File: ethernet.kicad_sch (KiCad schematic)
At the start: 57 parts, among them J4 WE-RJ45_7499111121A, U9 KSZ9031RNXCA, Y1 ABM8G-25.000MHZ-18-D2Y-T

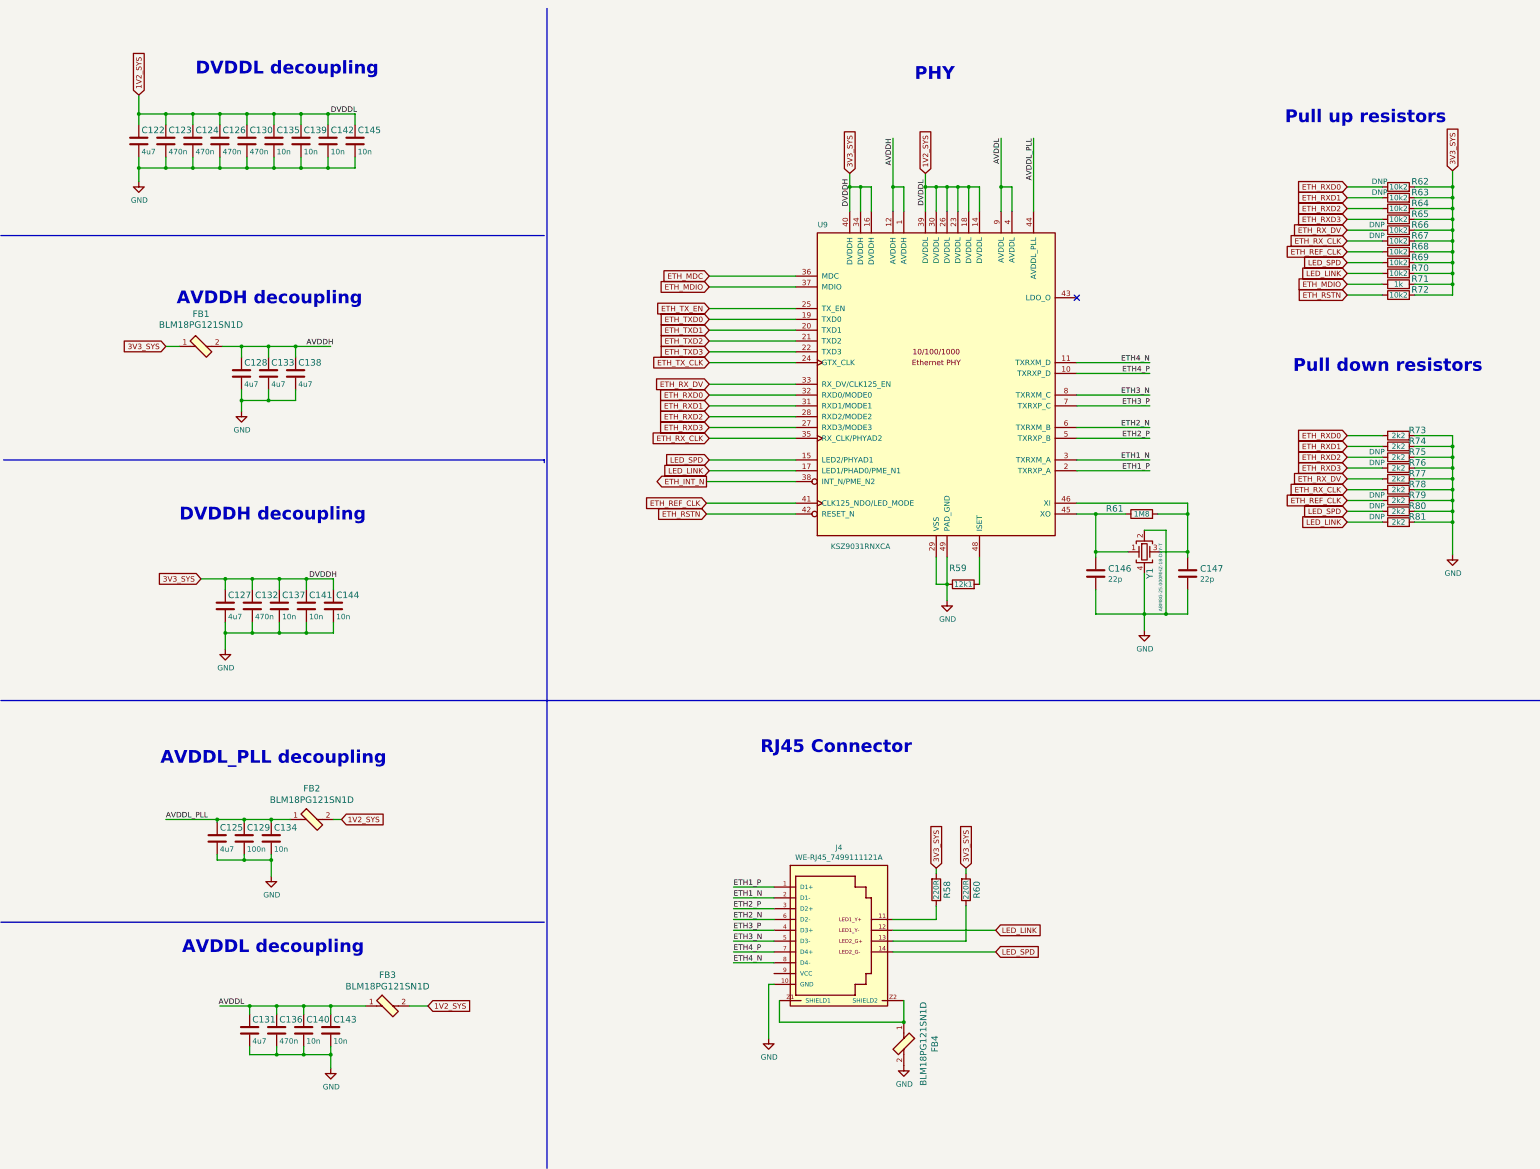
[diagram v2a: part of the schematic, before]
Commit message: Introduce component standarization
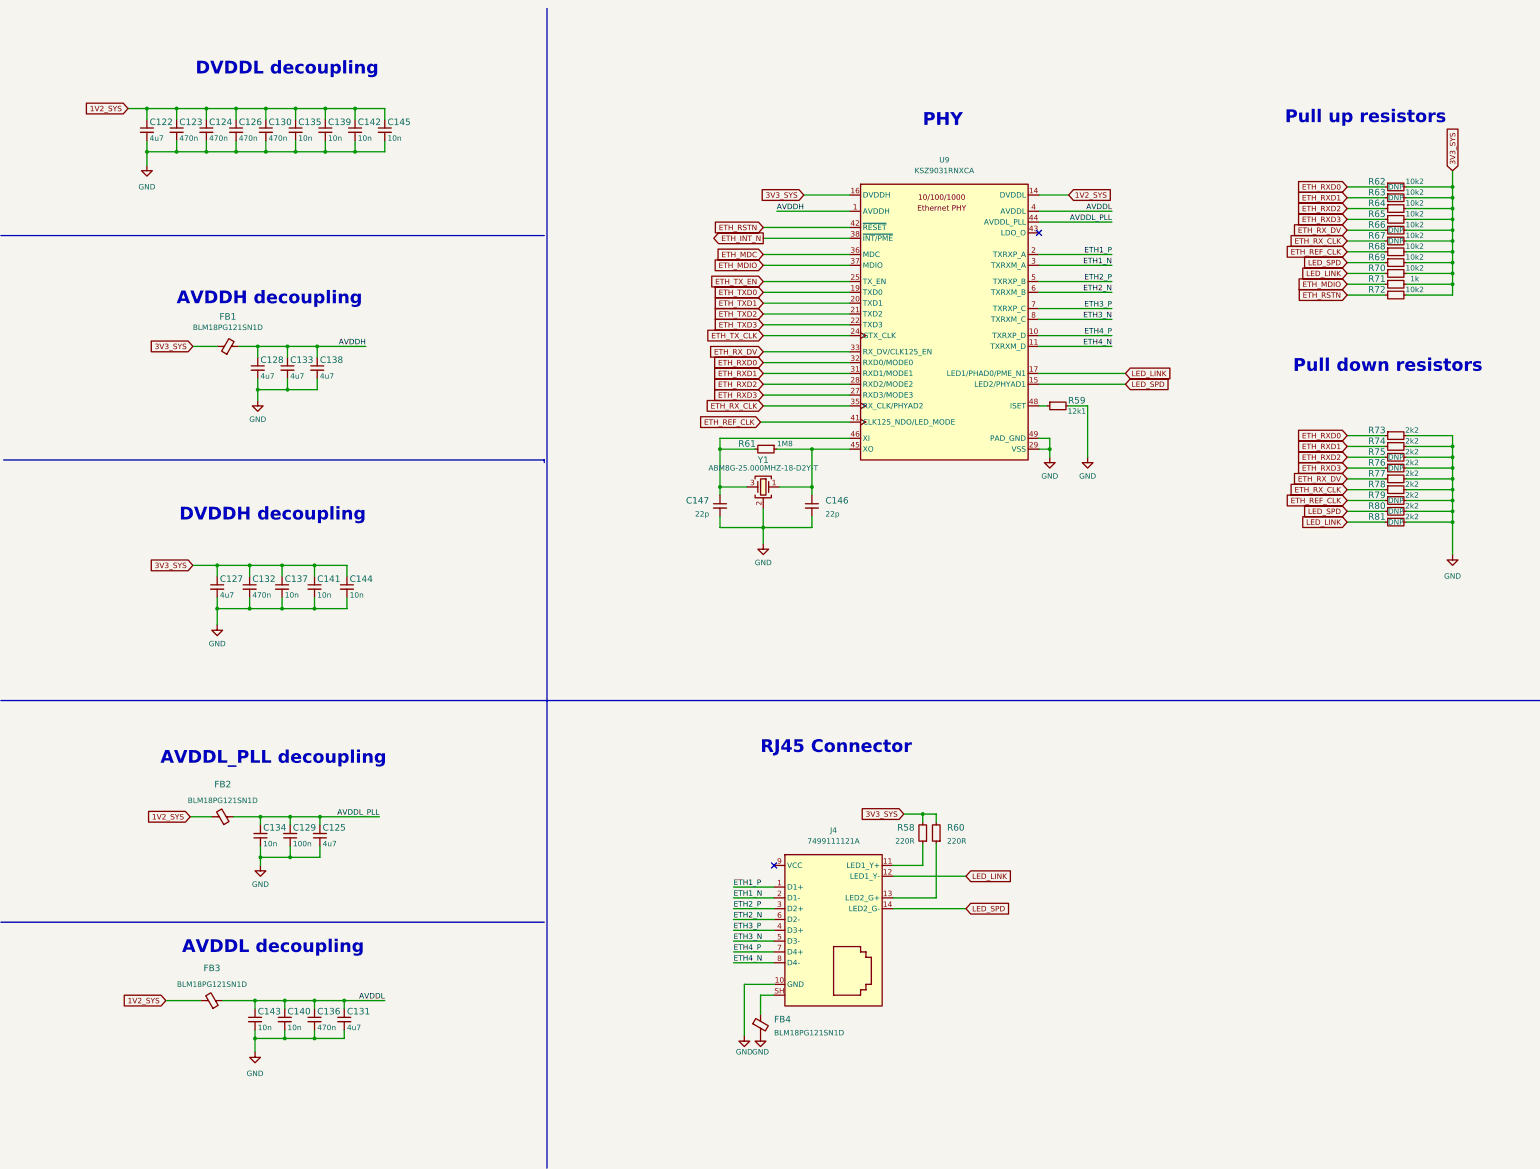
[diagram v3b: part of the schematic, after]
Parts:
- C122, C125, C127, C128, C131: footprint data-center-rdimm-ddr5-tester-footprints:0402-cap -> data-center-rdimm-ddr5-tester-footprints:C_0402_1005Metric; Author (none) -> Antmicro; License (none) -> Apache-2.0; Manufacturer MURATA -> Murata
- C123, C124, C126, C132, C136: footprint data-center-rdimm-ddr5-tester-footprints:0402-cap -> data-center-rdimm-ddr5-tester-footprints:C_0402_1005Metric; Author (none) -> Antmicro; License (none) -> Apache-2.0
- C129: value C_100n_0402 -> C_100n_16V_0402; footprint data-center-rdimm-ddr5-tester-footprints:0402-cap -> data-center-rdimm-ddr5-tester-footprints:C_0402_1005Metric; symbol data-center-rdimm-ddr5-tester:C_100n_0402_16V -> data-center-rdimm-ddr5-tester:C_100n_16V_0402; Author (none) -> Antmicro; License (none) -> Apache-2.0; Manufacturer MULTICOMP -> Multicomp
- C130: value C_10n_0402 -> C_470n_0402; footprint data-center-rdimm-ddr5-tester-footprints:0402-cap -> data-center-rdimm-ddr5-tester-footprints:C_0402_1005Metric; Author (none) -> Antmicro; License (none) -> Apache-2.0
- C133, C138: value C_10n_0402 -> C_4u7_0402; footprint data-center-rdimm-ddr5-tester-footprints:0402-cap -> data-center-rdimm-ddr5-tester-footprints:C_0402_1005Metric; Author (none) -> Antmicro; License (none) -> Apache-2.0; Manufacturer MURATA -> Murata
- C134, C135, C137, C139, C140, C141, C142, C143, C144, C145: footprint data-center-rdimm-ddr5-tester-footprints:0402-cap -> data-center-rdimm-ddr5-tester-footprints:C_0402_1005Metric; Author (none) -> Antmicro; Dielectric (none) -> X7R; License (none) -> Apache-2.0; MPN 04025G103ZAT2A -> GRM155R71H103KA88D; Manufacturer AVX -> Murata; Voltage (none) -> 50V
- C146, C147: footprint data-center-rdimm-ddr5-tester-footprints:0402-cap -> data-center-rdimm-ddr5-tester-footprints:C_0402_1005Metric; Author (none) -> Antmicro; License (none) -> Apache-2.0; Manufacturer YAGEO -> Yaego
- FB1, FB2, FB3, FB4: value BLM18PG121SN1D -> FB_120Z_2A_0603; footprint data-center-rdimm-ddr5-tester-footprints:0603-res -> data-center-rdimm-ddr5-tester-footprints:FB_0603_1608Metric; symbol data-center-rdimm-ddr5-tester:BLM18PG121SN1D -> data-center-rdimm-ddr5-tester:FB_120Z_2A_0603; Author (none) -> Antmicro; License (none) -> Apache-2.0; Manufacturer Murata Electronics North America -> Murata
- J4: value WE-RJ45_7499111121A -> Bus_RJ45_7499111121A; footprint data-center-rdimm-ddr5-tester-footprints:7499111121A -> data-center-rdimm-ddr5-tester-footprints:RJ45_7499111121A_Horizontal; symbol data-center-rdimm-ddr5-tester:WE-RJ45_7499111121A -> data-center-rdimm-ddr5-tester:Bus_RJ45_7499111121A; Author (none) -> Antmicro; License (none) -> Apache-2.0; Manufacturer WURTH ELEKTRONIK -> Würth Elektronik
- R58, R60: footprint data-center-rdimm-ddr5-tester-footprints:0402-res -> data-center-rdimm-ddr5-tester-footprints:R_0402_1005Metric; Author (none) -> Antmicro; License (none) -> Apache-2.0; MPN ERJ2GEJ221X -> CR0402-FX-2200GLF; Manufacturer Panasonic -> Bourns; Tolerance (none) -> 1%
- R59: footprint data-center-rdimm-ddr5-tester-footprints:0402-res -> data-center-rdimm-ddr5-tester-footprints:R_0402_1005Metric; Author (none) -> Antmicro; License (none) -> Apache-2.0; MPN MCWR04X1212FTL -> CR0402-FX-1212GLF; Manufacturer MULTICOMP -> Bourns; Tolerance (none) -> 1%
- R61: footprint data-center-rdimm-ddr5-tester-footprints:0402-res -> data-center-rdimm-ddr5-tester-footprints:R_0402_1005Metric; Author (none) -> Antmicro; License (none) -> Apache-2.0; MPN MCMR04X185_JTL -> CR0402-FX-1804GLF; Manufacturer MULTICOMP -> Bourns; Tolerance (none) -> 1%
- R62, R63, R64, R65, R66, R67, R68, R69, R70, R72: footprint data-center-rdimm-ddr5-tester-footprints:0402-res -> data-center-rdimm-ddr5-tester-footprints:R_0402_1005Metric; Author (none) -> Antmicro; License (none) -> Apache-2.0; MPN MCWR04X1022FTL -> CR0402-FX-1022GLF; Manufacturer MULTICOMP PRO -> Bourns; Tolerance (none) -> 1%
- R71: footprint data-center-rdimm-ddr5-tester-footprints:0402-res -> data-center-rdimm-ddr5-tester-footprints:R_0402_1005Metric; Author (none) -> Antmicro; License (none) -> Apache-2.0; Manufacturer BOURNS -> Bourns; Tolerance (none) -> 1%
- R73, R74, R75, R76, R77, R79, R80, R81: footprint data-center-rdimm-ddr5-tester-footprints:0402-res -> data-center-rdimm-ddr5-tester-footprints:R_0402_1005Metric; Author (none) -> Antmicro; License (none) -> Apache-2.0; MPN RC0402FR-072K2L -> CR0402-FX-2201GLF; Manufacturer YAGEO -> Bourns; Tolerance (none) -> 1%
- R78: footprint data-center-rdimm-ddr5-tester-footprints:0402-res -> data-center-rdimm-ddr5-tester-footprints:R_0402_1005Metric; Author (none) -> Antmicro; DNP DNP -> (none); License (none) -> Apache-2.0; MPN RC0402FR-072K2L -> CR0402-FX-2201GLF; Manufacturer YAGEO -> Bourns; Tolerance (none) -> 1%
- U9: footprint data-center-rdimm-ddr5-tester-footprints:QFN-48-Microchip-QFN77-48LD-PL-2 -> data-center-rdimm-ddr5-tester-footprints:QFN-48-1EP_7x7x0.9mm_P0.5mm_EP3.5x3.5mm; Author (none) -> Antmicro; License (none) -> Apache-2.0
- Y1: value ABM8G-25.000MHZ-18-D2Y-T -> Oscillator_SMD_25MHz_KX-7; footprint data-center-rdimm-ddr5-tester-footprints:KX-7 -> data-center-rdimm-ddr5-tester-footprints:Oscillator_SMD_Geyer_KX-7-4Pin_3.2x2.5mm; symbol data-center-rdimm-ddr5-tester:ABM8G-25.000MHZ-18-D2Y-T -> data-center-rdimm-ddr5-tester:Oscillator_SMD_25MHz_KX-7; Author (none) -> Antmicro; License (none) -> Apache-2.0; Val (none) -> 25MHz
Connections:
- net AVDDL_PLL: now also C125.2, C129.2, C134.2; no longer C125.1, C129.1, C134.1
- net GND: now also C125.1, C129.1, C134.1, R59.2; no longer C125.2, C129.2, C134.2, R59.1
- net at U9.13 (NC): now also U9.47 (NC)
- net at U9.48 (ISET): now also R59.1; no longer R59.2
- new net: FB4.1, J4.SH
- no-connect marks 1 -> 2
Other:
- moved on the sheet: C122, C123, C124, C125, C126, C127, C128, C129, C130, C131, C132, C133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

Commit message: [#55296] component update
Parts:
- FB1, FB2, FB3, FB4: symbol data-center-rdimm-ddr5-tester:FB_120Z_2A_0603 -> data-center-rdimm-ddr5-tester:FB_120Z_2A_Murata-BLM18PG_0603; Val (none) -> 120Z/2A
- R62, R63, R66, R67, R75, R76, R79, R80, R81: now not fitted; now left out of the parts list
- U9: Manufacturer Microchip -> Microchip Technology
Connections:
- net at U9.13 (NC): no longer U9.47 (NC)
